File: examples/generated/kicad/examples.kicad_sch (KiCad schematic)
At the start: 0 parts

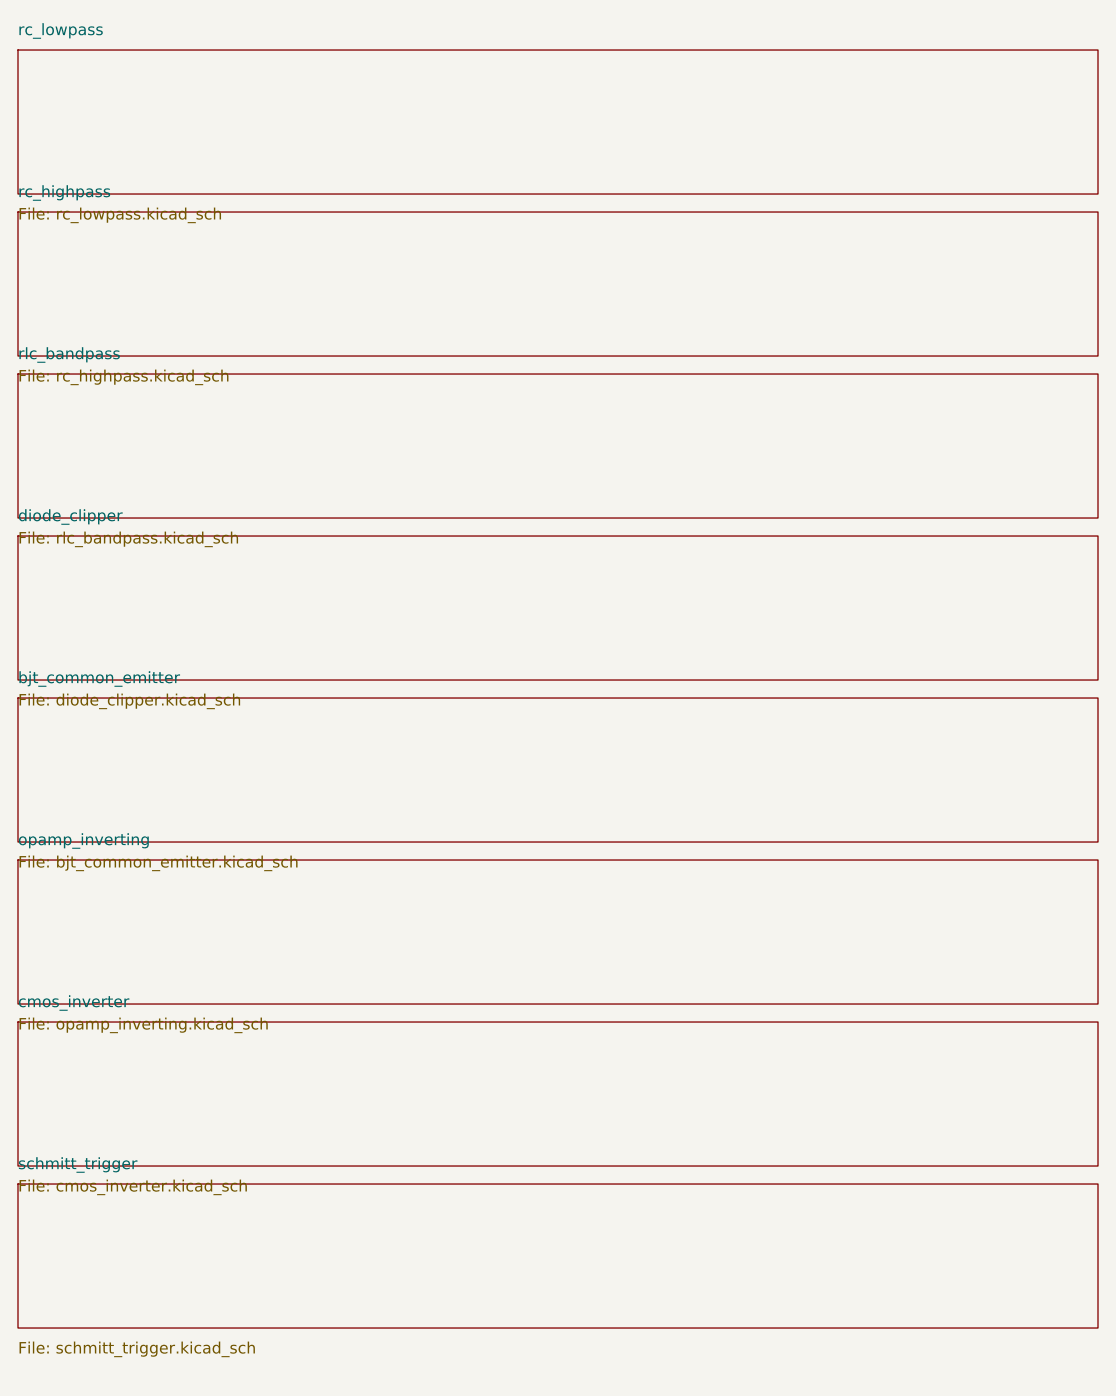
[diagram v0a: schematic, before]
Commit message: Attempt to clean up symbols and schematics to be more himan readable.
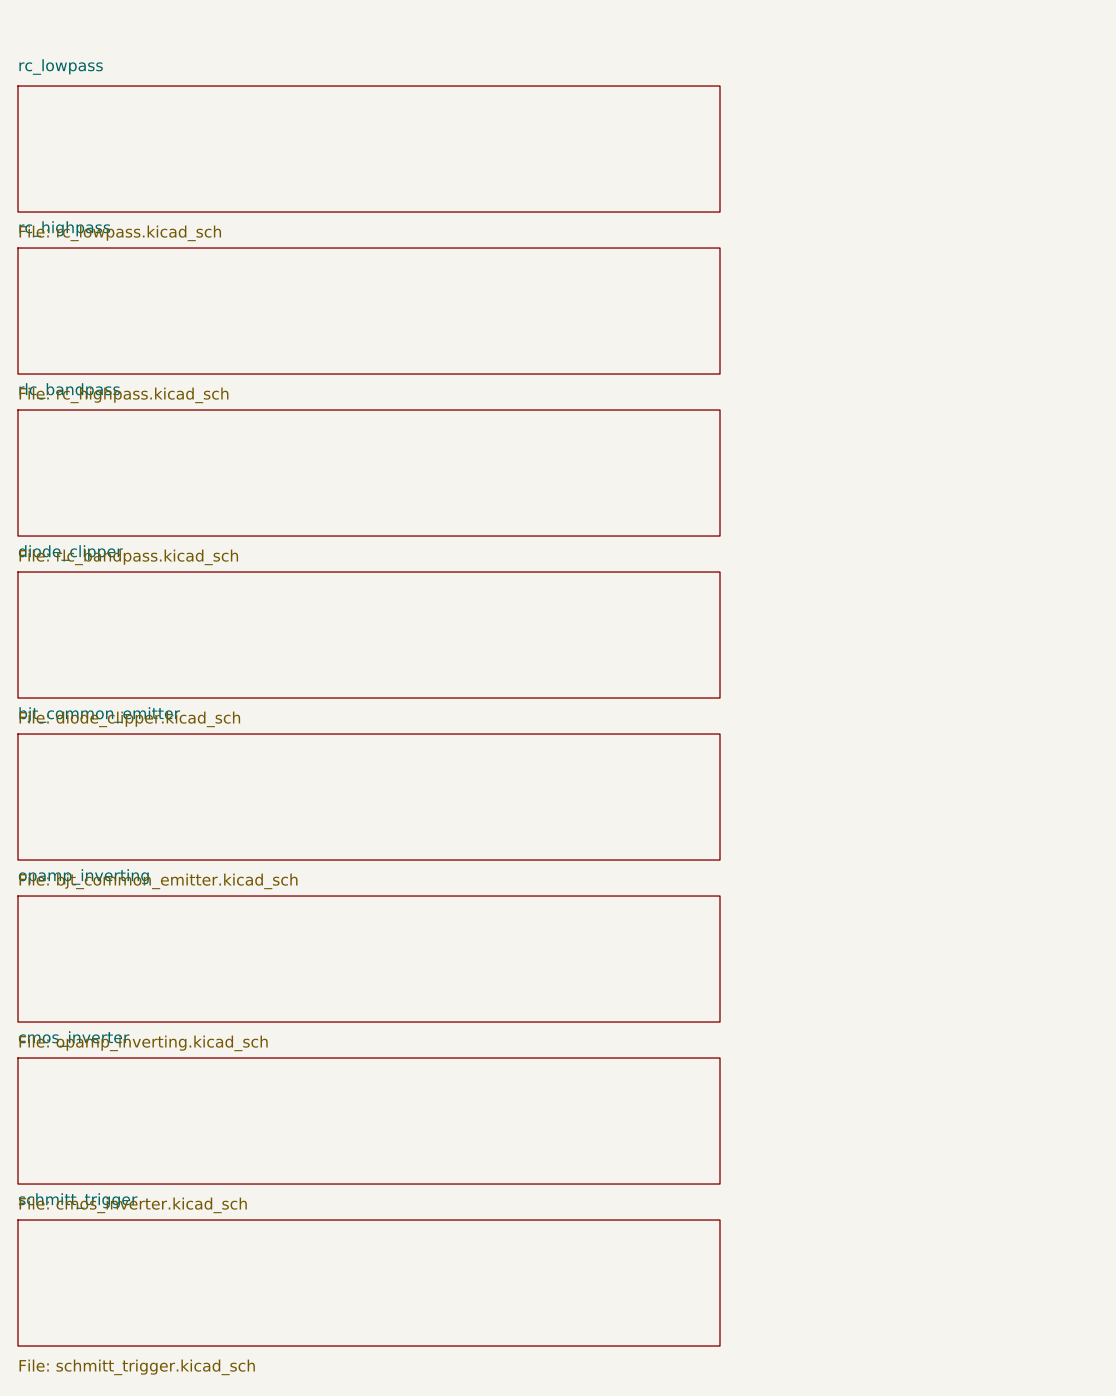
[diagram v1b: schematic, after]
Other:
- title: (none) -> mixedsig2cad examples
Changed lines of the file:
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@@
   (generator "mixedsig2cad")
   (paper "A4")
-  (sheet (at 25 20) (size 120 16)
+  (title_block
+    (title "mixedsig2cad examples")
+    (date "2026-03-05")
+    (comment 1 "Example sheet index")
+  )
+  (sheet (at 25 24) (size 78 14)
     (stroke (width 0) (type solid) (color 0 0 0 0))
     (fill (color 0 0 0 0))
-    (property "Sheet name" "rc_lowpass" (at 25 18.5 0)
+    (property "Sheet name" "rc_lowpass" (at 25 22.5 0)
       (effects (font (size 1.27 1.27)) (justify left bottom))
     )
-    (property "Sheet file" "rc_lowpass.kicad_sch" (at 25 37.5 0)
+    (property "Sheet file" "rc_lowpass.kicad_sch" (at 25 39.5 0)
       (effects (font (size 1.27 1.27)) (justify left top))
     )
   )
-  (sheet (at 25 38) (size 120 16)
+  (sheet (at 25 42) (size 78 14)
     (stroke (width 0) (type solid) (color 0 0 0 0))
     (fill (color 0 0 0 0))
-    (property "Sheet name" "rc_highpass" (at 25 36.5 0)
+    (property "Sheet name" "rc_highpass" (at 25 40.5 0)
       (effects (font (size 1.27 1.27)) (justify left bottom))
     )
-    (property "Sheet file" "rc_highpass.kicad_sch" (at 25 55.5 0)
+    (property "Sheet file" "rc_highpass.kicad_sch" (at 25 57.5 0)
       (effects (font (size 1.27 1.27)) (justify left top))
     )
   )
-  (sheet (at 25 56) (size 120 16)
+  (sheet (at 25 60) (size 78 14)
     (stroke (width 0) (type solid) (color 0 0 0 0))
     (fill (color 0 0 0 0))
-    (property "Sheet name" "rlc_bandpass" (at 25 54.5 0)
+    (property "Sheet name" "rlc_bandpass" (at 25 58.5 0)
       (effects (font (size 1.27 1.27)) (justify left bottom))
     )
-    (property "Sheet file" "rlc_bandpass.kicad_sch" (at 25 73.5 0)
+    (property "Sheet file" "rlc_bandpass.kicad_sch" (at 25 75.5 0)
       (effects (font (size 1.27 1.27)) (justify left top))
     )
   )
-  (sheet (at 25 74) (size 120 16)
+  (sheet (at 25 78) (size 78 14)
     (stroke (width 0) (type solid) (color 0 0 0 0))
     (fill (color 0 0 0 0))
-    (property "Sheet name" "diode_clipper" (at 25 72.5 0)
+    (property "Sheet name" "diode_clipper" (at 25 76.5 0)
       (effects (font (size 1.27 1.27)) (justify left bottom))
     )
-    (property "Sheet file" "diode_clipper.kicad_sch" (at 25 91.5 0)
+    (property "Sheet file" "diode_clipper.kicad_sch" (at 25 93.5 0)
       (effects (font (size 1.27 1.27)) (justify left top))
     )
   )
-  (sheet (at 25 92) (size 120 16)
+  (sheet (at 25 96) (size 78 14)
     (stroke (width 0) (type solid) (color 0 0 0 0))
     (fill (color 0 0 0 0))
-    (property "Sheet name" "bjt_common_emitter" (at 25 90.5 0)
+    (property "Sheet name" "bjt_common_emitter" (at 25 94.5 0)
       (effects (font (size 1.27 1.27)) (justify left bottom))
     )
-    (property "Sheet file" "bjt_common_emitter.kicad_sch" (at 25 109.5 0)
+    (property "Sheet file" "bjt_common_emitter.kicad_sch" (at 25 111.5 0)
       (effects (font (size 1.27 1.27)) (justify left top))
     )
   )
-  (sheet (at 25 110) (size 120 16)
+  (sheet (at 25 114) (size 78 14)
     (stroke (width 0) (type solid) (color 0 0 0 0))
     (fill (color 0 0 0 0))
-    (property "Sheet name" "opamp_inverting" (at 25 108.5 0)
+    (property "Sheet name" "opamp_inverting" (at 25 112.5 0)
       (effects (font (size 1.27 1.27)) (justify left bottom))
     )
-    (property "Sheet file" "opamp_inverting.kicad_sch" (at 25 127.5 0)
+    (property "Sheet file" "opamp_inverting.kicad_sch" (at 25 129.5 0)
       (effects (font (size 1.27 1.27)) (justify left top))
     )
   )
-  (sheet (at 25 128) (size 120 16)
+  (sheet (at 25 132) (size 78 14)
     (stroke (width 0) (type solid) (color 0 0 0 0))
     (fill (color 0 0 0 0))
-    (property "Sheet name" "cmos_inverter" (at 25 126.5 0)
+    (property "Sheet name" "cmos_inverter" (at 25 130.5 0)
       (effects (font (size 1.27 1.27)) (justify left bottom))
     )
-    (property "Sheet file" "cmos_inverter.kicad_sch" (at 25 145.5 0)
+    (property "Sheet file" "cmos_inverter.kicad_sch" (at 25 147.5 0)
       (effects (font (size 1.27 1.27)) (justify left top))
     )
   )
-  (sheet (at 25 146) (size 120 16)
+  (sheet (at 25 150) (size 78 14)
     (stroke (width 0) (type solid) (color 0 0 0 0))
     (fill (color 0 0 0 0))
-    (property "Sheet name" "schmitt_trigger" (at 25 144.5 0)
+    (property "Sheet name" "schmitt_trigger" (at 25 148.5 0)
       (effects (font (size 1.27 1.27)) (justify left bottom))
     )
-    (property "Sheet file" "schmitt_trigger.kicad_sch" (at 25 163.5 0)
+    (property "Sheet file" "schmitt_trigger.kicad_sch" (at 25 165.5 0)
       (effects (font (size 1.27 1.27)) (justify left top))
     )
